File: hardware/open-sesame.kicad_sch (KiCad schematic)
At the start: 9 parts, among them J1 Conn_01x10, J3 Barrel_Jack_Switch, J4 Conn_01x06_Socket

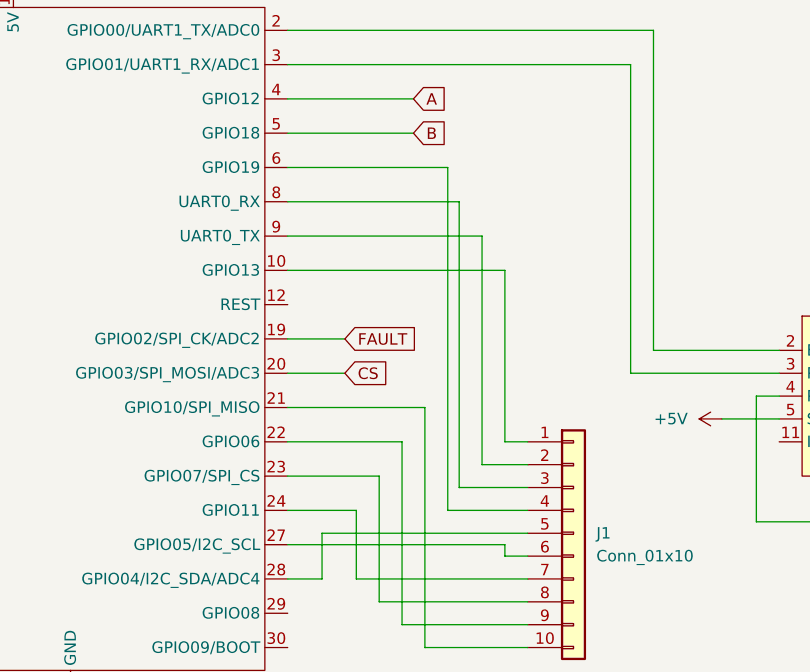
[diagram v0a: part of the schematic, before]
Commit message: Updated 3V & GND to terminal block
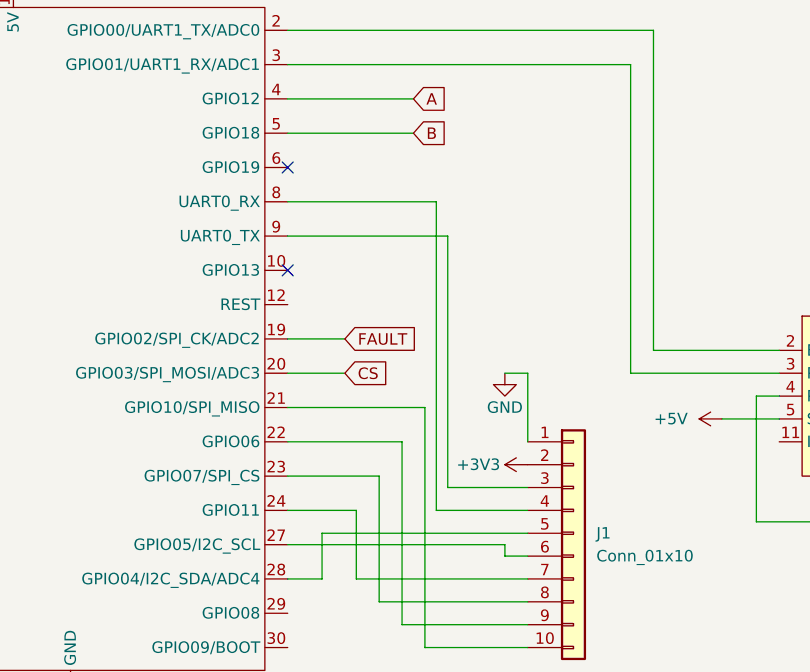
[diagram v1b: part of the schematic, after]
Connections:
- net +3V3: now also J1.2 (Pin_2)
- net GND: now also J1.1 (Pin_1)
- net at UESP32C3-CORE1.10 (GPIO13): no longer J1.1 (Pin_1)
- net at UESP32C3-CORE1.9 (UART0_TX): now also J1.3 (Pin_3); no longer J1.2 (Pin_2)
- net at UESP32C3-CORE1.8 (UART0_RX): now also J1.4 (Pin_4); no longer J1.3 (Pin_3)
- net at UESP32C3-CORE1.6 (GPIO19): no longer J1.4 (Pin_4)
- no-connect marks 2 -> 4
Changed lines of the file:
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@@
+	)
+	(no_connect
+		(at 95.25 100.33)
 	)
 	(no_connect
@@
 	)
 	(no_connect
+		(at 95.25 88.9)
+	)
+	(no_connect
 		(at 172.72 109.22)
 	)
 	(wire
 		(pts
-			(xy 119.38 100.33) (xy 119.38 119.38)
+			(xy 113.03 96.52) (xy 113.03 124.46)
 		)
 		(stroke
@@
 	(wire
 		(pts
-			(xy 95.25 100.33) (xy 119.38 100.33)
-		)
-		(stroke
-			(width 0)
-			(type default)
-		)
-	)
-	(wire
-		(pts
 			(xy 88.9 21.59) (xy 96.52 21.59)
 		)
@@
 	(wire
 		(pts
-			(xy 116.84 96.52) (xy 116.84 121.92)
-		)
-		(stroke
-			(width 0)
-			(type default)
-		)
-	)
-	(wire
-		(pts
 			(xy 146.05 30.48) (xy 151.13 30.48)
 		)
@@
 	(wire
 		(pts
-			(xy 113.03 88.9) (xy 113.03 127)
-		)
-		(stroke
-			(width 0)
-			(type default)
-		)
-	)
-	(wire
-		(pts
 			(xy 102.87 127) (xy 102.87 134.62)
 		)
@@
 	(wire
 		(pts
-			(xy 114.3 124.46) (xy 121.92 124.46)
-		)
-		(stroke
-			(width 0)
-			(type default)
-		)
-	)
-	(wire
-		(pts
 			(xy 99.06 134.62) (xy 99.06 129.54)
 		)
@@
 	(wire
 		(pts
-			(xy 114.3 92.71) (xy 114.3 124.46)
-		)
-		(stroke
-			(width 0)
-			(type default)
-		)
-	)
-	(wire
-		(pts
-			(xy 116.84 121.92) (xy 121.92 121.92)
-		)
-		(stroke
-			(width 0)
-			(type default)
-		)
-	)
-	(wire
-		(pts
-			(xy 95.25 96.52) (xy 116.84 96.52)
-		)
-		(stroke
-			(width 0)
-			(type default)
-		)
-	)
-	(wire
-		(pts
 			(xy 149.86 114.3) (xy 147.32 114.3)
 		)
@@
 	(wire
 		(pts
+			(xy 111.76 92.71) (xy 111.76 127)
+		)
+		(stroke
+			(width 0)
+			(type default)
+		)
+	)
+	(wire
+		(pts
 			(xy 50.8 31.75) (xy 53.34 31.75)
 		)
@@
 	(wire
 		(pts
-			(xy 113.03 127) (xy 121.92 127)
-		)
-		(stroke
-			(width 0)
-			(type default)
-		)
-	)
-	(wire
-		(pts
 			(xy 95.25 130.81) (xy 119.38 130.81)
 		)
@@
 	(wire
 		(pts
+			(xy 121.92 119.38) (xy 121.92 111.76)
+		)
+		(stroke
+			(width 0)
+			(type default)
+		)
+	)
+	(wire
+		(pts
 			(xy 147.32 128.27) (xy 160.02 128.27)
 		)
@@
 	(wire
 		(pts
+			(xy 111.76 127) (xy 121.92 127)
+		)
+		(stroke
+			(width 0)
+			(type default)
+		)
+	)
+	(wire
+		(pts
 			(xy 96.52 21.59) (xy 96.52 26.67)
 		)
@@
 	(wire
 		(pts
+			(xy 95.25 92.71) (xy 111.76 92.71)
+		)
+		(stroke
+			(width 0)
+			(type default)
+		)
+	)
+	(wire
+		(pts
 			(xy 161.29 99.06) (xy 161.29 102.87)
 		)
@@
 	(wire
 		(pts
+			(xy 95.25 96.52) (xy 113.03 96.52)
+		)
+		(stroke
+			(width 0)
+			(type default)
+		)
+	)
+	(wire
+		(pts
 			(xy 105.41 123.19) (xy 105.41 137.16)
 		)
@@
 	(wire
 		(pts
-			(xy 95.25 92.71) (xy 114.3 92.71)
-		)
-		(stroke
-			(width 0)
-			(type default)
-		)
-	)
-	(wire
-		(pts
 			(xy 162.56 125.73) (xy 162.56 128.27)
 		)
@@
 	(wire
 		(pts
-			(xy 95.25 88.9) (xy 113.03 88.9)
+			(xy 121.92 111.76) (xy 119.38 111.76)
 		)
 		(stroke
@@
 	(wire
 		(pts
-			(xy 119.38 119.38) (xy 121.92 119.38)
+			(xy 113.03 124.46) (xy 121.92 124.46)
 		)
 		(stroke
@@
 	(symbol
 		(lib_id "power:GND")
+		(at 119.38 111.76 0)
+		(unit 1)
+		(exclude_from_sim no)
+		(in_bom yes)
+		(on_board yes)
+		(dnp no)
+		(property "Reference" "#PWR08"
+			(at 119.38 118.11 0)
+			(effects
+				(font
+					(size 1.27 1.27)
+				)
+				(hide yes)
+			)
+		)
+		(property "Value" "GND"
+			(at 119.38 115.57 0)
+			(effects
+				(font
+					(size 1.27 1.27)
+				)
+			)
+		)
+		(property "Footprint" ""
+			(at 119.38 111.76 0)
+			(effects
+				(font
+					(size 1.27 1.27)
+				)
+				(hide yes)
+			)
+		)
+		(property "Datasheet" ""
+			(at 119.38 111.76 0)
+			(effects
+				(font
+					(size 1.27 1.27)
+				)
+				(hide yes)
+			)
+		)
+		(property "Description" "Power symbol creates a global label with name \"GND\" , ground"
+			(at 119.38 111.76 0)
+			(effects
+				(font
+					(size 1.27 1.27)
+				)
+				(hide yes)
+			)
+		)
+		(pin "1"
+		)
+		(instances
+			(project ""
+				(path "/0083c209-1745-4c16-a7cf-90b66eccdd04"
+					(reference "#PWR08")
+					(unit 1)
+				)
+			)
+		)
+	)
+	(symbol
+		(lib_id "power:GND")
 		(at 160.02 130.81 0)
 		(unit 1)
@@
 					(unit 1)
 				)
+			)
+		)
+	)
+	(symbol
+		(lib_id "power:+3V3")
+		(at 121.92 121.92 90)
+		(unit 1)
+		(exclude_from_sim no)
+		(in_bom yes)
+		(on_board yes)
+		(dnp no)
+		(property "Reference" "#PWR09"
+			(at 125.73 121.92 0)
+			(effects
+				(font
+					(size 1.27 1.27)
+				)
+				(hide yes)
+			)
+		)
+		(property "Value" "+3V3"
+			(at 118.872 121.92 90)
+			(effects
+				(font
+					(size 1.27 1.27)
+				)
+				(justify left)
+			)
+		)
+		(property "Footprint" ""
+			(at 121.92 121.92 0)
+			(effects
+				(font
+					(size 1.27 1.27)
+				)
+				(hide yes)
+			)
+		)
+		(property "Datasheet" ""
+			(at 121.92 121.92 0)
+			(effects
+				(font
+					(size 1.27 1.27)
+				)
+				(hide yes)
+			)
+		)
+		(property "Description" "Power symbol creates a global label with name \"+3V3\""
+			(at 121.92 121.92 0)
+			(effects
+				(font
+					(size 1.27 1.27)
+				)
+				(hide yes)
+			)
+		)
+		(pin "1"
+		)
+		(instances
+			(project "ferrous-oxslide2"
+				(path "/0083c209-1745-4c16-a7cf-90b66eccdd04"
+					(reference "#PWR09")
+					(unit 1)
+				)

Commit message: fix(hardware): Corrected VIN&VOUT
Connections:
- net +24V: now also D45V5F3.1 (VOUT); no longer D45V5F3.3 (VIN)
- net +3V3: now also D45V5F3.3 (VIN); no longer D45V5F3.1 (VOUT)
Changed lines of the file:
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@@
 	(symbol
 		(lib_id "power:+24V")
-		(at 30.48 31.75 90)
+		(at 53.34 31.75 270)
 		(unit 1)
 		(exclude_from_sim no)
@@
 		(fields_autoplaced yes)
 		(property "Reference" "#PWR01"
-			(at 34.29 31.75 0)
+			(at 49.53 31.75 0)
 			(effects
 				(font
@@
 		)
 		(property "Value" "+24V"
-			(at 26.67 31.7499 90)
+			(at 57.15 31.7499 90)
 			(effects
 				(font
@@
 		)
 		(property "Footprint" ""
-			(at 30.48 31.75 0)
-			(effects
-				(font
-					(size 1.27 1.27)
-				)
-				(hide yes)
-			)
-		)
-		(property "Datasheet" ""
-			(at 30.48 31.75 0)
+			(at 53.34 31.75 0)
+			(effects
+				(font
+					(size 1.27 1.27)
+				)
+				(hide yes)
+			)
+		)
+		(property "Datasheet" ""
+			(at 53.34 31.75 0)
 			(effects
 				(font
@@
 		)
 		(property "Description" "Power symbol creates a global label with name \"+24V\""
-			(at 30.48 31.75 0)
-			(effects
-				(font
-					(size 1.27 1.27)
-				)
-				(hide yes)
-			)
-		)
-		(pin "1"
-		)
-		(instances
-			(project "ferrous-oxslide2"
+			(at 53.34 31.75 0)
+			(effects
+				(font
+					(size 1.27 1.27)
+				)
+				(hide yes)
+			)
+		)
+		(pin "1"
+		)
+		(instances
+			(project "open-sesame"
 				(path "/0083c209-1745-4c16-a7cf-90b66eccdd04"
 					(reference "#PWR01")
@@
 	(symbol
 		(lib_id "power:+3V3")
-		(at 53.34 31.75 270)
+		(at 30.48 31.75 90)
 		(unit 1)
 		(exclude_from_sim no)
@@
 		(fields_autoplaced yes)
 		(property "Reference" "#PWR04"
-			(at 49.53 31.75 0)
+			(at 34.29 31.75 0)
 			(effects
 				(font
@@
 		)
 		(property "Value" "+3V3"
-			(at 57.15 31.7499 90)
-			(effects
-				(font
-					(size 1.27 1.27)
-				)
-				(justify left)
+			(at 29.21 29.21 90)
+			(effects
+				(font
+					(size 1.27 1.27)
+				)
 			)
 		)
 		(property "Footprint" ""
-			(at 53.34 31.75 0)
-			(effects
-				(font
-					(size 1.27 1.27)
-				)
-				(hide yes)
-			)
-		)
-		(property "Datasheet" ""
-			(at 53.34 31.75 0)
+			(at 30.48 31.75 0)
+			(effects
+				(font
+					(size 1.27 1.27)
+				)
+				(hide yes)
+			)
+		)
+		(property "Datasheet" ""
+			(at 30.48 31.75 0)
 			(effects
 				(font
@@
 		)
 		(property "Description" "Power symbol creates a global label with name \"+3V3\""
-			(at 53.34 31.75 0)
-			(effects
-				(font
-					(size 1.27 1.27)
-				)
-				(hide yes)
-			)
-		)
-		(pin "1"
-		)
-		(instances
-			(project ""
+			(at 30.48 31.75 0)
+			(effects
+				(font
+					(size 1.27 1.27)
+				)
+				(hide yes)
+			)
+		)
+		(pin "1"
+		)
+		(instances
+			(project "open-sesame"
 				(path "/0083c209-1745-4c16-a7cf-90b66eccdd04"
 					(reference "#PWR04")

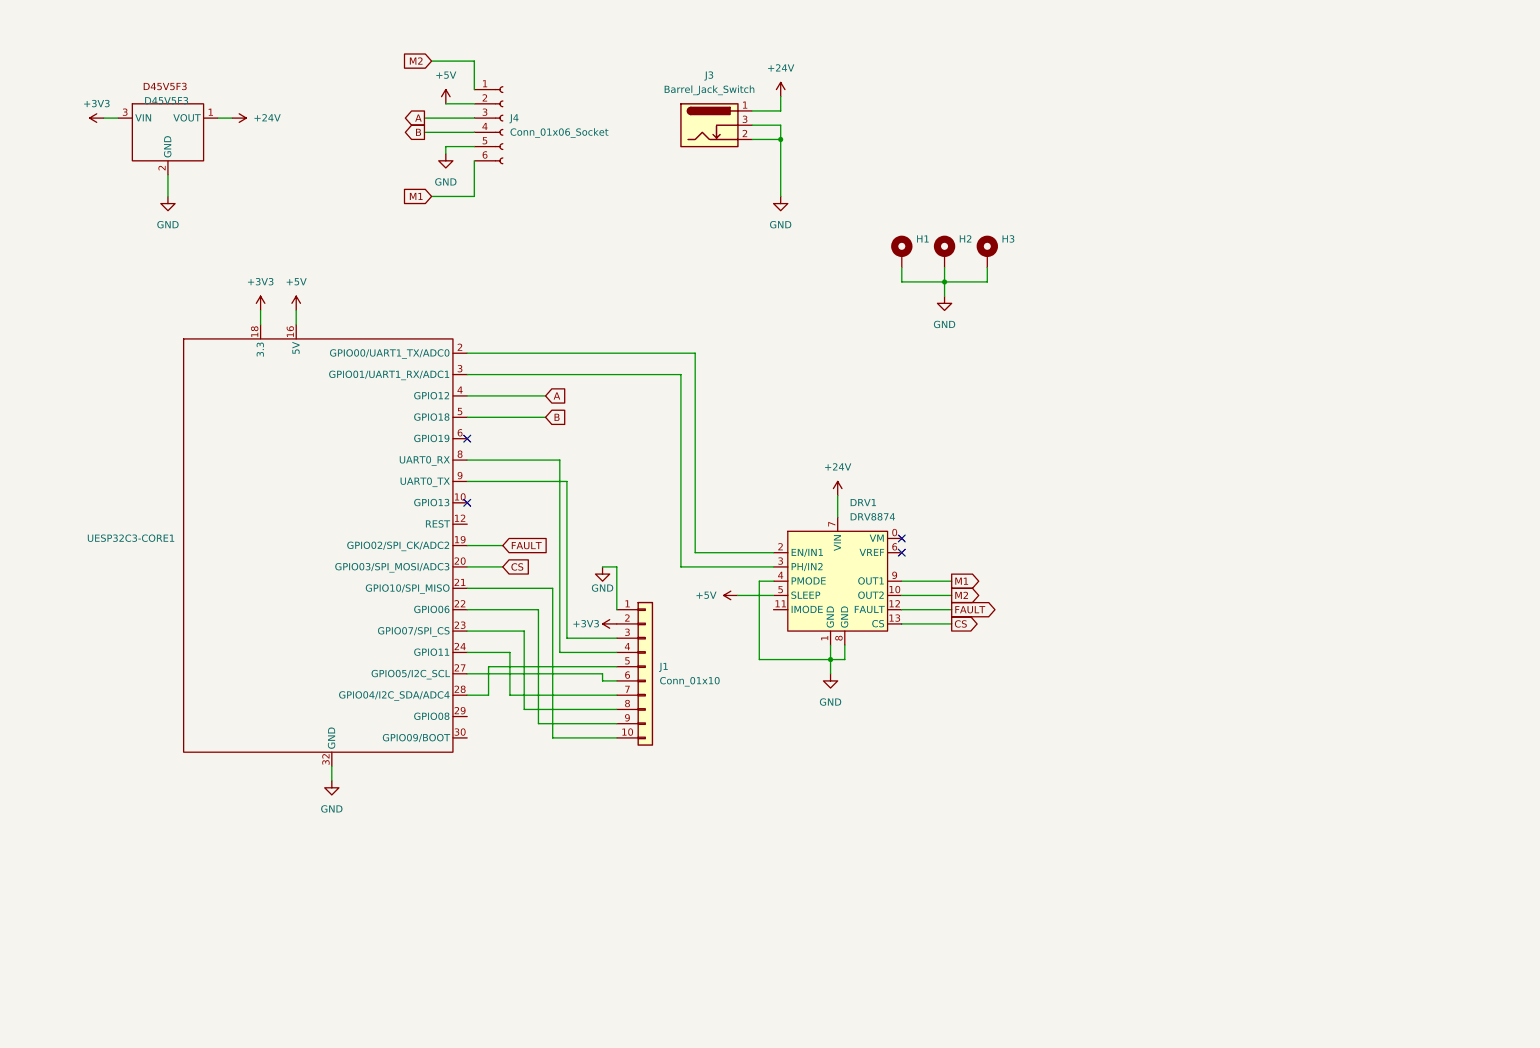
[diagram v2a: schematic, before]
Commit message: User Terminals, Added Optocoupler, Added QWIIC connector
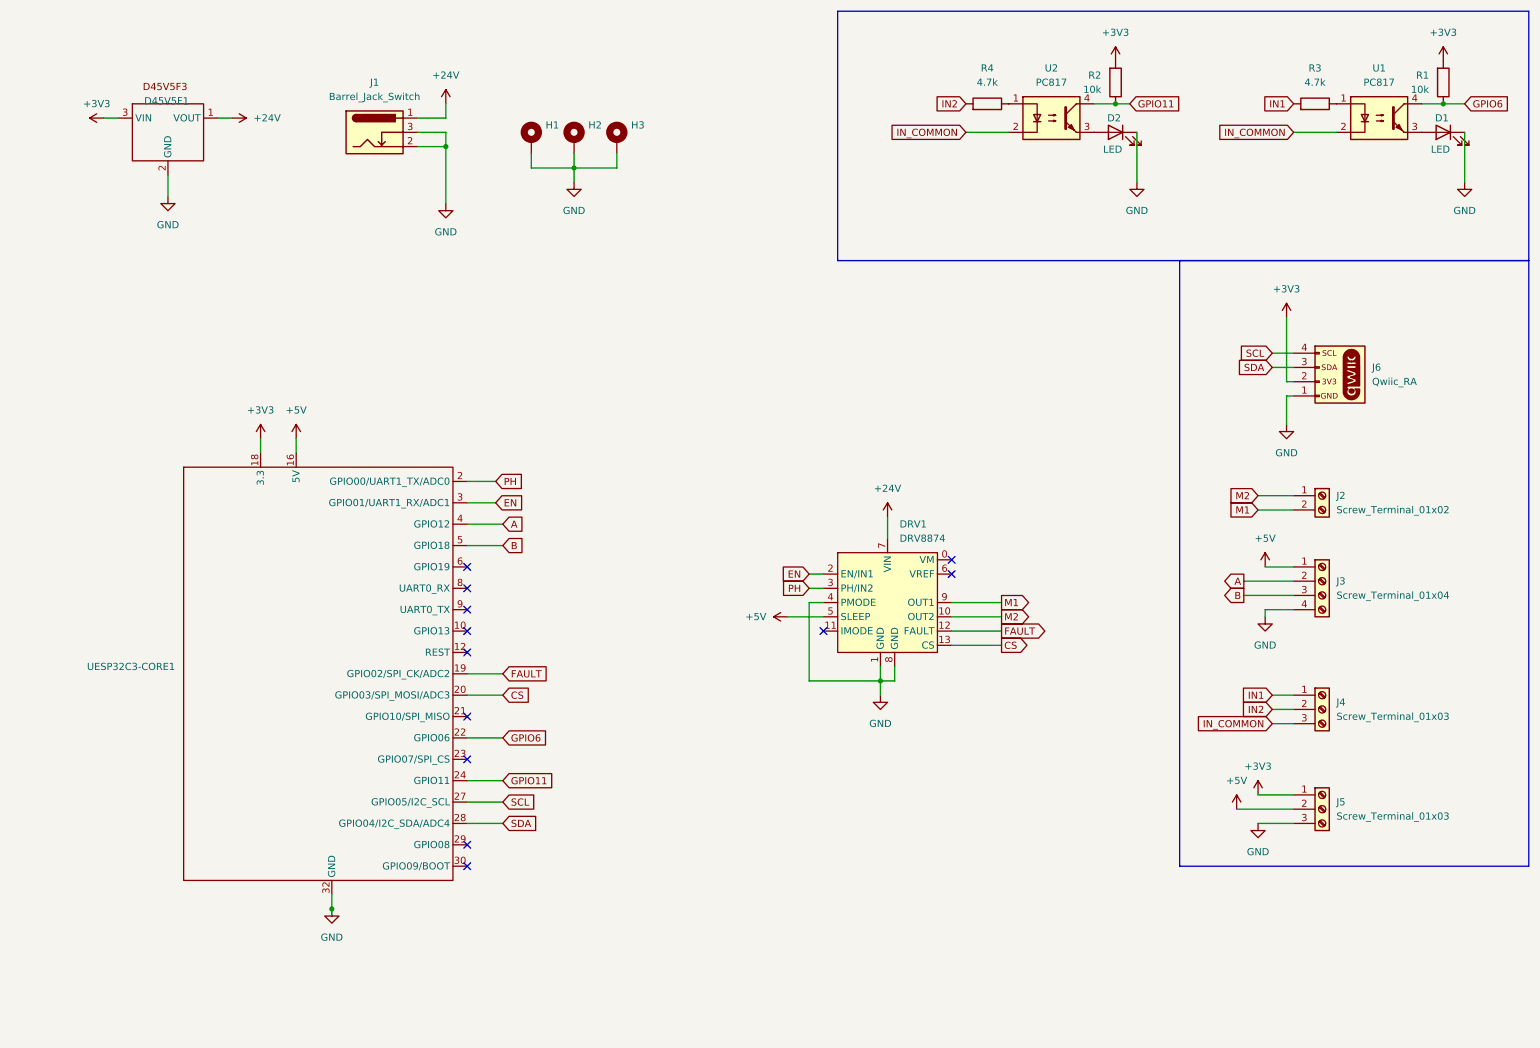
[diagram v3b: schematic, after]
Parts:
- removed J1: Conn_01x10, MyLibrary:TerminalBlock_TE_1-282834-0_1x10_P2.54mm_Horizontal, symbol Connector_Generic:Conn_01x10
- removed J4: Conn_01x06_Socket, Connector_JST:JST_PH_S6B-PH-K_1x06_P2.00mm_Horizontal, symbol Connector:Conn_01x06_Socket
- added D1, D2: LED, LED_SMD:LED_0603_1608Metric, symbol Device:LED
- added J2: Screw_Terminal_01x02, MyLibrary:TE_282834-2, symbol Connector:Screw_Terminal_01x02
- added J3: Screw_Terminal_01x04, MyLibrary:TE_282834-4, symbol Connector:Screw_Terminal_01x04
- added J4, J5: Screw_Terminal_01x03, MyLibrary:TE_282834-3, symbol Connector:Screw_Terminal_01x03
- added J6: Qwiic_RA, SparkFun-Connector:JST_1x04_P1.0mm_Horizontal_SMD, symbol SparkFun-Connector:Qwiic_Horizontal
- added R1, R2: 10k, Resistor_SMD:R_0603_1608Metric, symbol Device:R
- added R3, R4: 4.7k, Resistor_SMD:R_0603_1608Metric, symbol Device:R
- added U1, U2: PC817, Package_DIP:DIP-4_W7.62mm, symbol Isolator:PC817
- D45V5F1: renamed from D45V5F3; footprint Library:D45V5Fx -> MyLibrary:D45V5Fx
- DRV1: footprint Library:DRV8874 -> MyLibrary:DRV8874
- UESP32C3-CORE1: footprint Library:LUATOS_ESP32C3 -> MyLibrary:LUATOS_ESP32C3
- renumbered J3 to J1
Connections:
- net +3V3: now also J5.1 (Pin_1), J6.2 (Pin_2), R1.2, R2.2
- net +5V: now also J3.1 (Pin_1), J5.2 (Pin_2)
- net A: now also J3.2 (Pin_2)
- net B: now also J3.3 (Pin_3)
- net GND: now also D1.1 (K), D2.1 (K), J3.4 (Pin_4), J5.3 (Pin_3), J6.1 (Pin_1)
- net M1: now also J2.2 (Pin_2)
- net M2: now also J2.1 (Pin_1)
- net EN: now reaches DRV1.2 (EN/IN1)
- net EN: now also UESP32C3-CORE1.3 (GPIO01/UART1_RX/ADC1); no longer UESP32C3-CORE1.2 (GPIO00/UART1_TX/ADC0)
- net PH: now reaches DRV1.3 (PH/IN2)
- net PH: now also UESP32C3-CORE1.2 (GPIO00/UART1_TX/ADC0); no longer UESP32C3-CORE1.3 (GPIO01/UART1_RX/ADC1)
- net SDA: now reaches UESP32C3-CORE1.28 (GPIO04/I2C_SDA/ADC4)
- net SDA: now also J6.3 (Pin_3)
- net SCL: now reaches UESP32C3-CORE1.27 (GPIO05/I2C_SCL)
- net SCL: now also J6.4 (Pin_4)
- net GPIO11: now reaches UESP32C3-CORE1.24 (GPIO11)
- net GPIO11: now also R2.1, U2.4
- net GPIO6: now reaches UESP32C3-CORE1.22 (GPIO06)
- net GPIO6: now also R1.1, U1.4
- new net: D2.2 (A), U2.3
- new net: R3.1, U1.1
- new net: D1.2 (A), U1.3
- new net: R4.1, U2.1
- new net IN1: J4.1 (Pin_1), R3.2
- new net IN2: J4.2 (Pin_2), R4.2
- new net IN_COMMON: J4.3 (Pin_3), U1.2, U2.2
- no-connect marks 4 -> 12
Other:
- moved on the sheet: DRV1, H1, H2, H3, J1, UESP32C3-CORE1
